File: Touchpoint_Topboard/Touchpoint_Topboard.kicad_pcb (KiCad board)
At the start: 2 copper layers, 51 x 96.4 mm, 29 parts, among them J1 Conn_01x03, J2 Conn_01x03, J3 Conn_01x10, J4 EC10E1220501, Q1 NMOS, SW3 SW_SPST, U1 LT3750AEMS-TRPBF, U101 AS78L05RTR-E1, U201 DA2032-AL

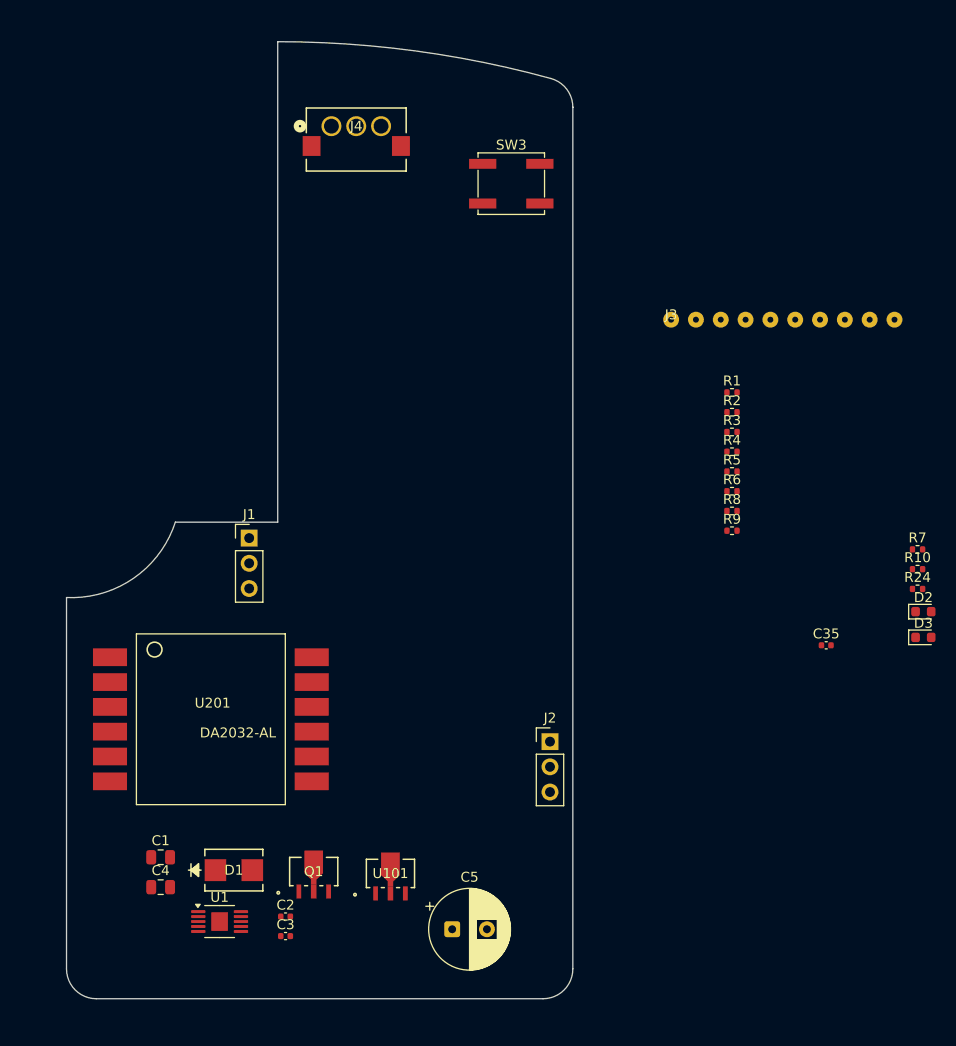
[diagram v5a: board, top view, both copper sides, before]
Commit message: Finished Routing and Placement of Top Board
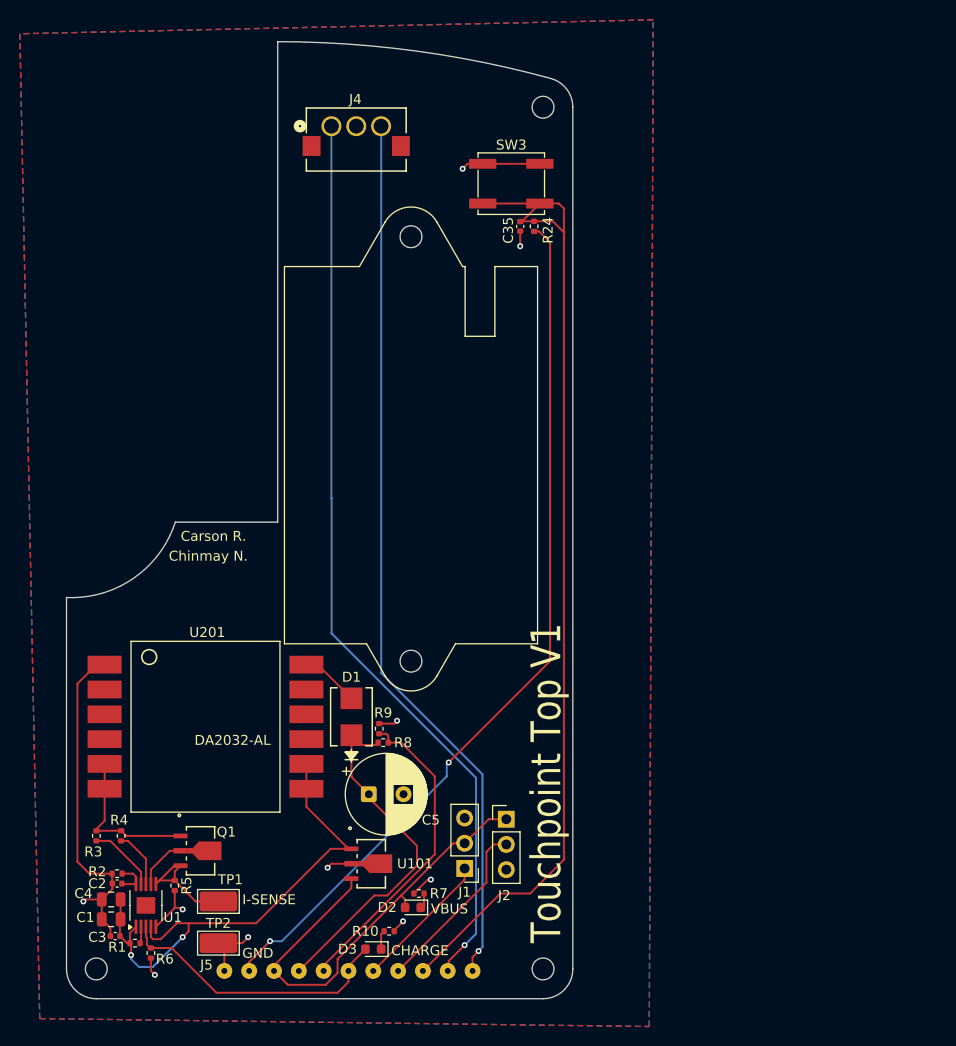
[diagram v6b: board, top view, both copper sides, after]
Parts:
- removed J3: Conn_01x10, Touchpoint:Jumper_Interface_10
- added J5: Conn_01x11, Touchpoint:Jumper_Interface_11, F.Cu at (40.4, 113.6)
- added REF**: MountingHole_2.2mm_M2, MountingHole:MountingHole_2.2mm_M2, F.Cu at (72.5, 26.6)
- added REF**: MountingHole_2.2mm_M2, MountingHole:MountingHole_2.2mm_M2, F.Cu at (72.5, 113.4)
- added REF**: MountingHole_2.2mm_M2, MountingHole:MountingHole_2.2mm_M2, F.Cu at (27.5, 113.4)
- added REF**: Servo_Mount, Touchpoint:Servo_Mount, F.Cu at (50.0, 20.0)
- added TP1: TestPoint, TestPoint:TestPoint_Keystone_5019_Miniature, F.Cu at (39.8, 106.6)
- added TP2: TestPoint, TestPoint:TestPoint_Keystone_5019_Miniature, F.Cu at (39.8, 110.8)
- moved R1 81.8 mm to (31.4, 110.8)
- moved R2 77.4 mm to (29.6, 103.8), turned to 180 degrees
- moved R3 75.9 mm to (27.5, 100.0), turned to 90 degrees
- moved R6 74.8 mm to (33.0, 111.8), turned to 90 degrees
- moved R4 72.7 mm to (30.0, 100.0), turned to 90 degrees
- moved R5 69.9 mm to (35.4, 105.0), turned to 90 degrees
- moved R10 64.5 mm to (57.0, 109.6)
- moved D3 63.7 mm to (55.4, 111.4), turned to 180 degrees
- moved R7 61.0 mm to (60.0, 105.8), turned to 180 degrees
- moved D2 59.4 mm to (59.4, 107.2), turned to 180 degrees
- moved R24 53.2 mm to (71.6, 38.6), turned to 90 degrees
- moved C35 52.3 mm to (70.2, 38.6), turned to -90 degrees
- moved R8 42.2 mm to (56.4, 90.6), turned to 180 degrees
- moved R9 40.7 mm to (56.0, 89.2), turned to -90 degrees
- moved J1 39.7 mm to (64.6, 103.3), turned to 180 degrees
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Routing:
- net /RCLICK: track 0.00 -> 101.0 mm
- net /SCROLLA: track 0.00 -> 92.3 mm, vias 0 -> 1
- net /SCROLLB: track 0.00 -> 89.7 mm, vias 0 -> 1
- net +3.3V: track 0.00 -> 88.7 mm, vias 0 -> 2
- net GND: track 0.00 -> 66.4 mm, vias 0 -> 10
- net +5V: track 0.00 -> 52.7 mm, vias 0 -> 2
- net VBUS: track 0.00 -> 45.8 mm
- net VPP: track 0.00 -> 35.6 mm
- net /VREF: track 0.00 -> 32.2 mm
- net /CHARGE: track 0.00 -> 28.6 mm
- net /NEOPIXEL: track 0.00 -> 18.0 mm
- net Net-(Q1-D): track 0.00 -> 15.8 mm
- net /SERVO: track 0.00 -> 14.1 mm
- net Net-(Q1-S): track 0.00 -> 12.3 mm
- net Net-(U1-RVOUT): track 0.00 -> 7.02 mm
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- added copper zone on B.Cu, net GND
- added copper zone on F.Cu, net GND
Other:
- board text added: "CHARGE"
- board text added: "Carson R."
- board text added: "Chinmay N."
- board text added: "GND"
- board text added: "I-SENSE"
- board text added: "Touchpoint Top V1"
- board text added: "VBUS"

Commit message: Added Via Stitching and Changed VBUS Trace
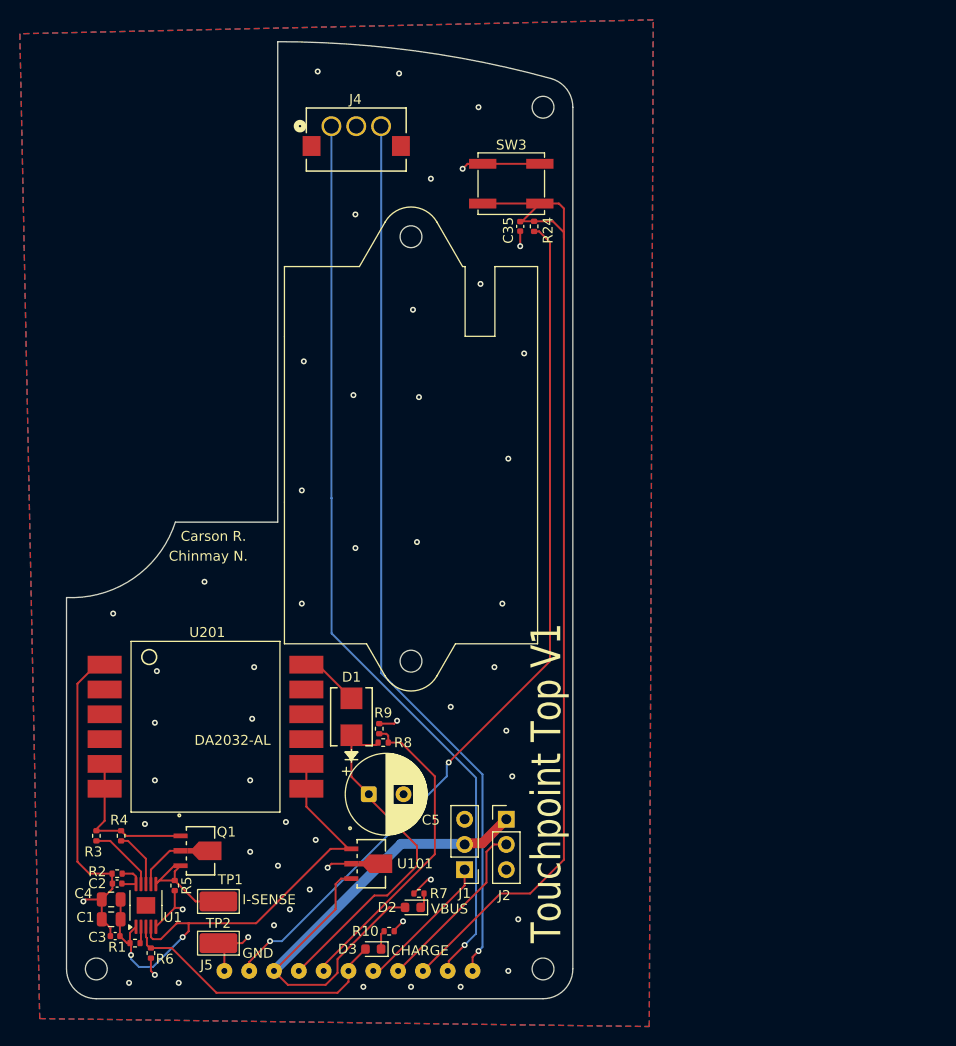
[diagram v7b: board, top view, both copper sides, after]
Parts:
- moved J1 0.12 mm to (64.6, 103.4)
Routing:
- net VBUS: track 45.8 -> 60.8 mm
- net GND: vias 10 -> 54

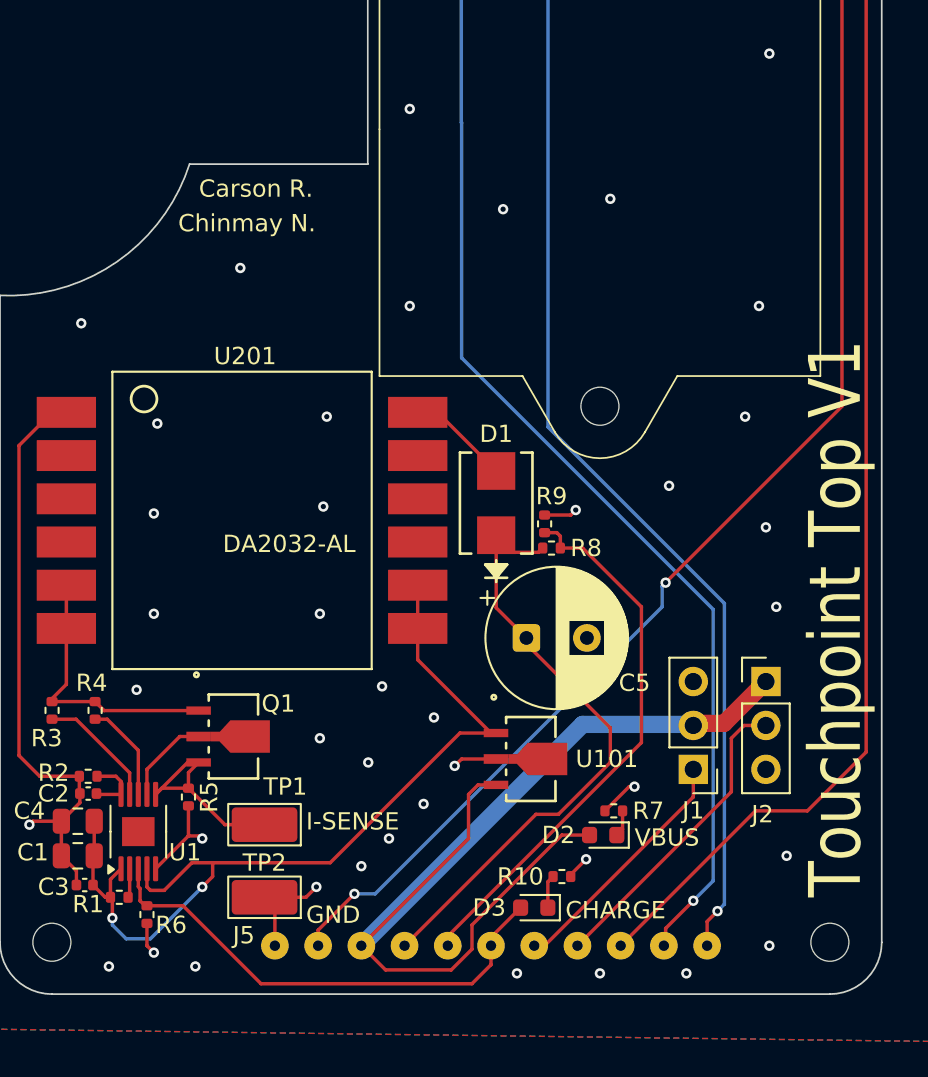
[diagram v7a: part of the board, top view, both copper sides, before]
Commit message: Finished silkscreening
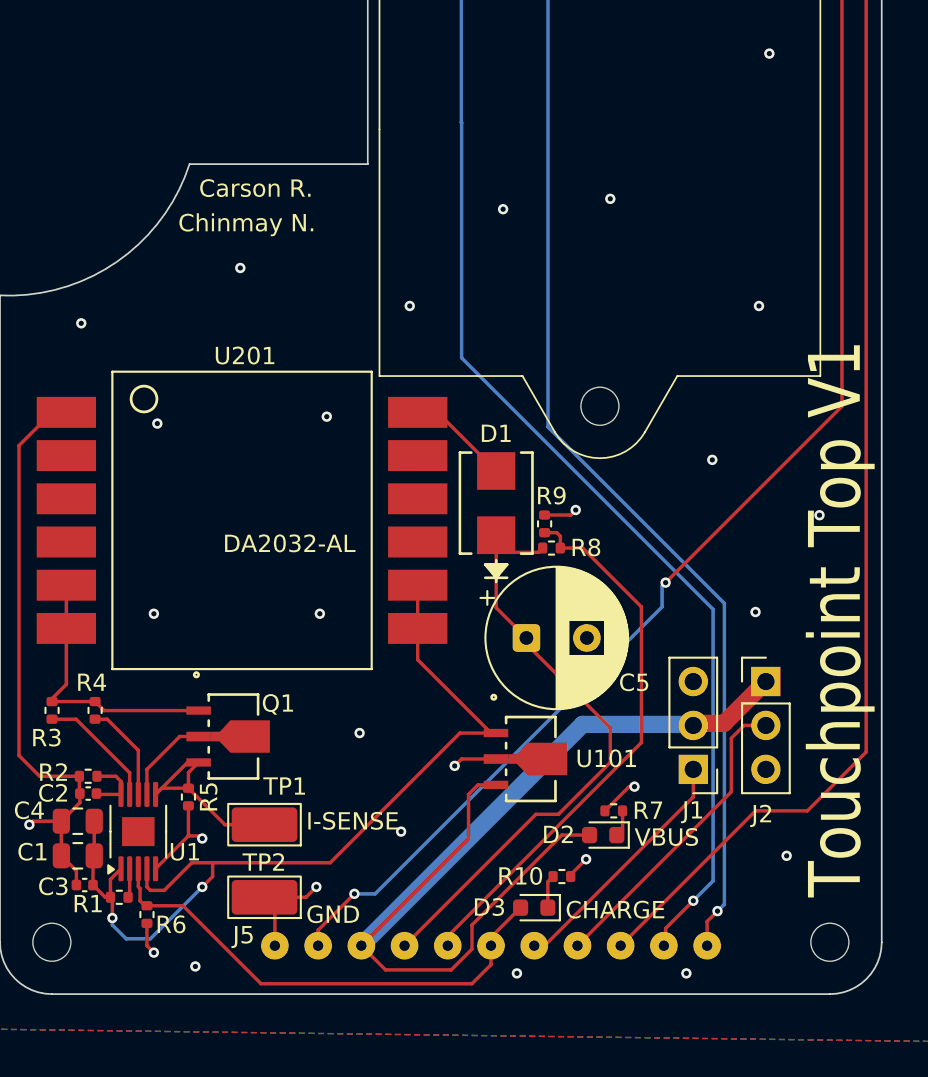
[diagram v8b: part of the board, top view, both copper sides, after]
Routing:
- net GND: vias 54 -> 41
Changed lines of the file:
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@@
 			(font
 				(size 1 1)
-				(thickness 0.1)
+				(thickness 0.15)
 			)
 			(justify left bottom)
@@
 			(font
 				(size 1 1)
-				(thickness 0.1)
+				(thickness 0.15)
 			)
 			(justify left bottom)
@@
 			(font
 				(size 1 1)
-				(thickness 0.1)
+				(thickness 0.15)
 			)
 			(justify left bottom)
@@
 			(font
 				(size 1 1)
-				(thickness 0.1)
+				(thickness 0.15)
 			)
 			(justify left bottom)
@@
 			(font
 				(size 1 1)
-				(thickness 0.1)
+				(thickness 0.15)
 			)
 			(justify left bottom)
@@
 			(font
 				(size 1 1)
-				(thickness 0.1)
+				(thickness 0.15)
 			)
 			(justify left bottom)
@@
 	)
 	(via
-		(at 48.2 65.2)
-		(size 0.6)
-		(drill 0.3)
-		(layers "F.Cu" "B.Cu")
-		(net 1)
-	)
-	(via
 		(at 70 108.4)
 		(size 0.6)
@@
 	)
 	(via
-		(at 68.8 89.4)
-		(size 0.6)
-		(drill 0.3)
-		(layers "F.Cu" "B.Cu")
-		(net 1)
-	)
-	(via
-		(at 59.2 115.2)
-		(size 0.6)
-		(drill 0.3)
-		(layers "F.Cu" "B.Cu")
-		(net 1)
-	)
-	(via
-		(at 45.8 103)
+		(at 71.9 88.7)
 		(size 0.6)
 		(drill 0.3)
@@
 	)
 	(via
-		(at 47 107.4)
-		(size 0.6)
-		(drill 0.3)
-		(layers "F.Cu" "B.Cu")
-		(net 1)
-	)
-	(via
 		(at 43.4 83)
 		(size 0.6)
@@
 	)
 	(via
-		(at 63.2 87)
-		(size 0.6)
-		(drill 0.3)
-		(layers "F.Cu" "B.Cu")
-		(net 1)
-	)
-	(via
-		(at 45.4 109)
-		(size 0.6)
-		(drill 0.3)
-		(layers "F.Cu" "B.Cu")
-		(net 1)
-	)
-	(via
-		(at 69 113.6)
+		(at 65.7 85.5)
+		(size 0.6)
+		(drill 0.3)
+		(layers "F.Cu" "B.Cu")
+		(net 1)
+	)
+	(via
+		(at 47.7 107)
 		(size 0.6)
 		(drill 0.3)
@@
 	)
 	(via
-		(at 33.4 88.6)
-		(size 0.6)
-		(drill 0.3)
-		(layers "F.Cu" "B.Cu")
-		(net 1)
-	)
-	(via
 		(at 43 94.4)
 		(size 0.6)
@@
 	)
 	(via
-		(at 46.6 98.6)
-		(size 0.6)
-		(drill 0.3)
-		(layers "F.Cu" "B.Cu")
-		(net 1)
-	)
-	(via
-		(at 30.8 114.8)
-		(size 0.6)
-		(drill 0.3)
-		(layers "F.Cu" "B.Cu")
-		(net 1)
-	)
-	(via
 		(at 49.8 23)
 		(size 0.6)
@@
 	)
 	(via
-		(at 49 105.4)
-		(size 0.6)
-		(drill 0.3)
-		(layers "F.Cu" "B.Cu")
-		(net 1)
-	)
-	(via
-		(at 49.6 100.4)
-		(size 0.6)
-		(drill 0.3)
-		(layers "F.Cu" "B.Cu")
-		(net 1)
-	)
-	(via
 		(at 29.2 77.6)
 		(size 0.6)
@@
 	)
 	(via
-		(at 67.6 83)
-		(size 0.6)
-		(drill 0.3)
-		(layers "F.Cu" "B.Cu")
-		(net 1)
-	)
-	(via
-		(at 32.4 98.8)
-		(size 0.6)
-		(drill 0.3)
-		(layers "F.Cu" "B.Cu")
-		(net 1)
-	)
-	(via
 		(at 58 23.2)
 		(size 0.6)
@@
 	)
 	(via
-		(at 43 101.6)
-		(size 0.6)
-		(drill 0.3)
-		(layers "F.Cu" "B.Cu")
-		(net 1)
-	)
-	(via
-		(at 69.4 94)
+		(at 45.3 101.3)
+		(size 0.6)
+		(drill 0.3)
+		(layers "F.Cu" "B.Cu")
+		(net 1)
+	)
+	(via
+		(at 68.2 94.3)
 		(size 0.6)
 		(drill 0.3)
@@
 		(size 0.6)
 		(drill 0.3)
-		(layers "F.Cu" "B.Cu")
-		(net 1)
-	)
-	(via
-		(at 43.2 88.2)
-		(size 0.6)
-		(drill 0.3)
